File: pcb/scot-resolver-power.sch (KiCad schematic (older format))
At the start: 42 parts, among them IC4 TSR1, U1 MCP1703A-5002_SOT223, U2 LT1762, U3 MCP1703A-5002_SOT223, U4 MCP1703A-5002_SOT223, U5 MCP1703A-3302_SOT223

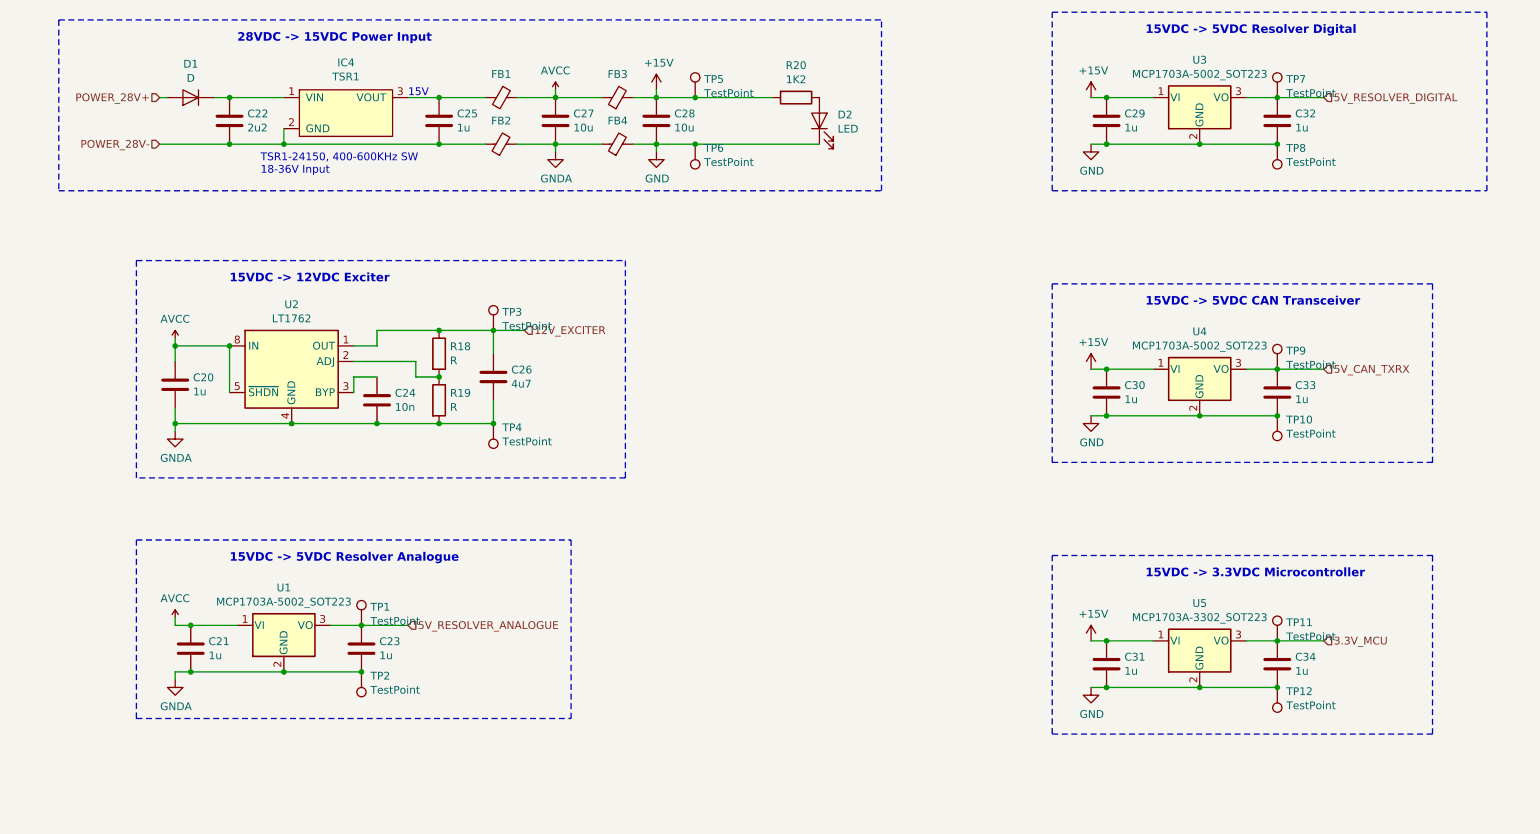
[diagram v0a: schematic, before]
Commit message: PCB Progress, laying tracks.
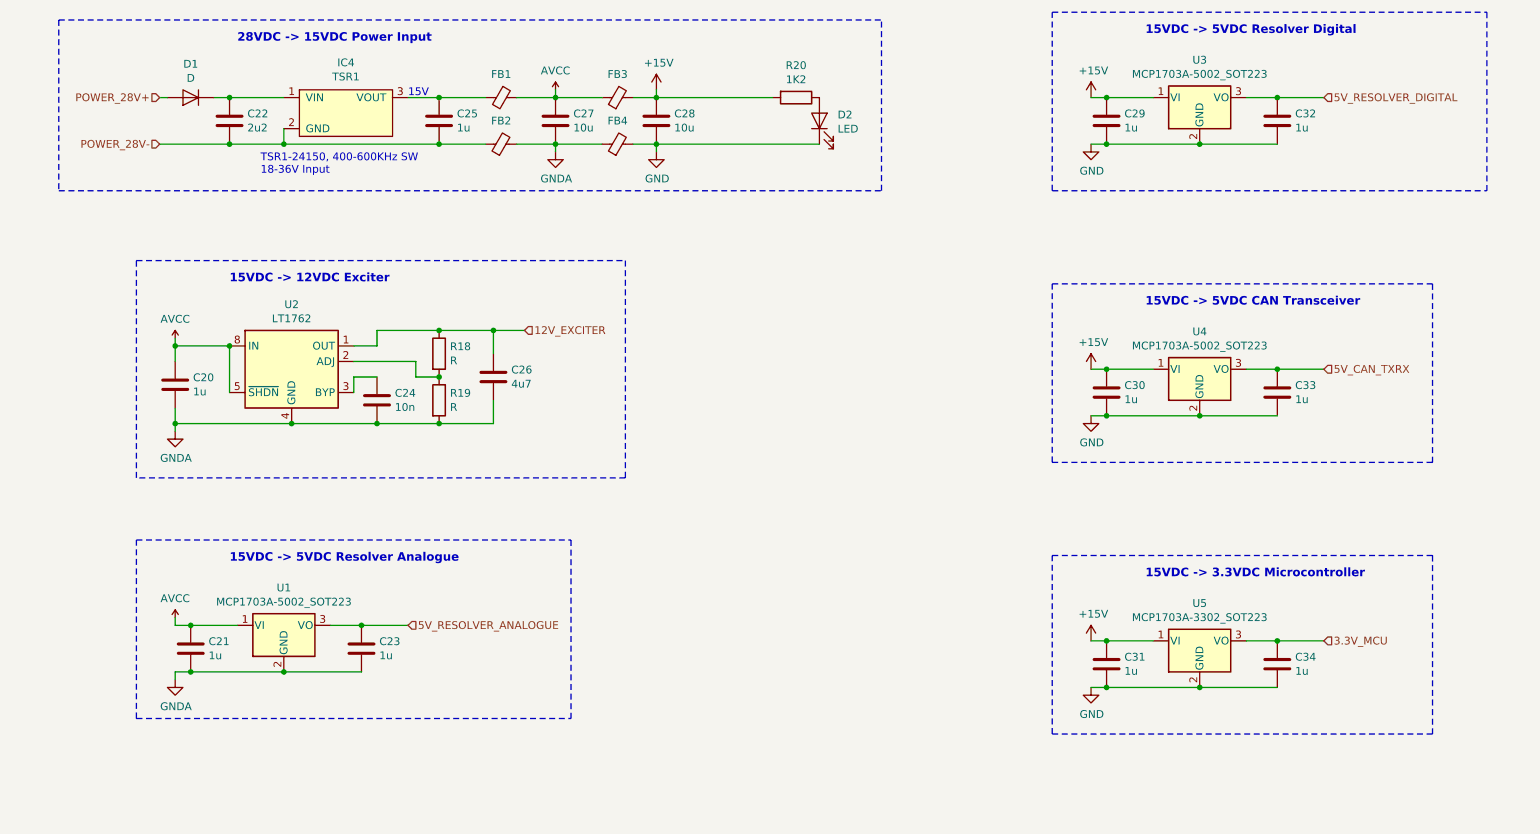
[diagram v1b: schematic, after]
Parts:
- removed TP1, TP10, TP11, TP12, TP2, TP3, TP4, TP5, TP6, TP7, TP8, TP9: TestPoint, TestPoint:TestPoint_Pad_D2.0mm, symbol Connector:TestPoint
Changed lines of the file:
@@
 Connection ~ 3250 3800
-Wire Wire Line
-	4000 3650 4000 3800
-Wire Wire Line
-	4000 3800 3650 3800
-Connection ~ 3650 3800
 Wire Wire Line
 	4000 3350 4000 3200
@@
 	1950 5100 1950 5050
 $Comp
-L Connector:TestPoint TP5
-U 1 1 5E584815
-P 5300 1700
-F 0 "TP5" H 5358 1818 50  0000 L CNN
-F 1 "TestPoint" H 5358 1727 50  0000 L CNN
-F 2 "TestPoint:TestPoint_Pad_D2.0mm" H 5500 1700 50  0001 C CNN
-F 3 "~" H 5500 1700 50  0001 C CNN
-	1    5300 1700
-	1    0    0    -1
-$EndComp
-$Comp
-L Connector:TestPoint TP6
-U 1 1 5E58568E
-P 5300 2000
-F 0 "TP6" H 5242 2026 50  0000 R CNN
-F 1 "TestPoint" H 5242 2117 50  0000 R CNN
-F 2 "TestPoint:TestPoint_Pad_D2.0mm" H 5500 2000 50  0001 C CNN
-F 3 "~" H 5500 2000 50  0001 C CNN
-	1    5300 2000
-	-1   0    0    1
-$EndComp
-Wire Wire Line
-	5050 2000 5300 2000
-Wire Wire Line
-	5050 1700 5300 1700
-$Comp
-L Connector:TestPoint TP3
-U 1 1 5E59AD0B
-P 4000 3200
-F 0 "TP3" H 4058 3318 50  0000 L CNN
-F 1 "TestPoint" H 4058 3227 50  0000 L CNN
-F 2 "TestPoint:TestPoint_Pad_D2.0mm" H 4200 3200 50  0001 C CNN
-F 3 "~" H 4200 3200 50  0001 C CNN
-	1    4000 3200
-	1    0    0    -1
-$EndComp
-$Comp
-L Connector:TestPoint TP4
-U 1 1 5E59B3ED
-P 4000 3800
-F 0 "TP4" H 3942 3826 50  0000 R CNN
-F 1 "TestPoint" H 3942 3917 50  0000 R CNN
-F 2 "TestPoint:TestPoint_Pad_D2.0mm" H 4200 3800 50  0001 C CNN
-F 3 "~" H 4200 3800 50  0001 C CNN
-	1    4000 3800
-	-1   0    0    1
-$EndComp
-Connection ~ 4000 3800
-$Comp
-L Connector:TestPoint TP1
-U 1 1 5E59C88E
-P 3150 5100
-F 0 "TP1" H 3208 5218 50  0000 L CNN
-F 1 "TestPoint" H 3208 5127 50  0000 L CNN
-F 2 "TestPoint:TestPoint_Pad_D2.0mm" H 3350 5100 50  0001 C CNN
-F 3 "~" H 3350 5100 50  0001 C CNN
-	1    3150 5100
-	1    0    0    -1
-$EndComp
-$Comp
-L Connector:TestPoint TP2
-U 1 1 5E59D052
-P 3150 5400
-F 0 "TP2" H 3092 5426 50  0000 R CNN
-F 1 "TestPoint" H 3092 5517 50  0000 R CNN
-F 2 "TestPoint:TestPoint_Pad_D2.0mm" H 3350 5400 50  0001 C CNN
-F 3 "~" H 3350 5400 50  0001 C CNN
-	1    3150 5400
-	-1   0    0    1
-$EndComp
-Connection ~ 3150 5400
-$Comp
-L Connector:TestPoint TP7
-U 1 1 5E59E980
-P 9050 1700
-F 0 "TP7" H 9108 1818 50  0000 L CNN
-F 1 "TestPoint" H 9108 1727 50  0000 L CNN
-F 2 "TestPoint:TestPoint_Pad_D2.0mm" H 9250 1700 50  0001 C CNN
-F 3 "~" H 9250 1700 50  0001 C CNN
-	1    9050 1700
-	1    0    0    -1
-$EndComp
-$Comp
-L Connector:TestPoint TP8
-U 1 1 5E5A080B
-P 9050 2000
-F 0 "TP8" H 8992 2026 50  0000 R CNN
-F 1 "TestPoint" H 8992 2117 50  0000 R CNN
-F 2 "TestPoint:TestPoint_Pad_D2.0mm" H 9250 2000 50  0001 C CNN
-F 3 "~" H 9250 2000 50  0001 C CNN
-	1    9050 2000
-	-1   0    0    1
-$EndComp
-Connection ~ 9050 2000
-$Comp
-L Connector:TestPoint TP10
-U 1 1 5E5A264B
-P 9050 3750
-F 0 "TP10" H 8992 3776 50  0000 R CNN
-F 1 "TestPoint" H 8992 3867 50  0000 R CNN
-F 2 "TestPoint:TestPoint_Pad_D2.0mm" H 9250 3750 50  0001 C CNN
-F 3 "~" H 9250 3750 50  0001 C CNN
-	1    9050 3750
-	-1   0    0    1
-$EndComp
-Connection ~ 9050 3750
-$Comp
-L Connector:TestPoint TP9
-U 1 1 5E5A2ECC
-P 9050 3450
-F 0 "TP9" H 9108 3568 50  0000 L CNN
-F 1 "TestPoint" H 9108 3477 50  0000 L CNN
-F 2 "TestPoint:TestPoint_Pad_D2.0mm" H 9250 3450 50  0001 C CNN
-F 3 "~" H 9250 3450 50  0001 C CNN
-	1    9050 3450
-	1    0    0    -1
-$EndComp
-$Comp
-L Connector:TestPoint TP12
-U 1 1 5E5A4134
-P 9050 5500
-F 0 "TP12" H 8992 5526 50  0000 R CNN
-F 1 "TestPoint" H 8992 5617 50  0000 R CNN
-F 2 "TestPoint:TestPoint_Pad_D2.0mm" H 9250 5500 50  0001 C CNN
-F 3 "~" H 9250 5500 50  0001 C CNN
-	1    9050 5500
-	-1   0    0    1
-$EndComp
-Connection ~ 9050 5500
-$Comp
-L Connector:TestPoint TP11
-U 1 1 5E5A4624
-P 9050 5200
-F 0 "TP11" H 9108 5318 50  0000 L CNN
-F 1 "TestPoint" H 9108 5227 50  0000 L CNN
-F 2 "TestPoint:TestPoint_Pad_D2.0mm" H 9250 5200 50  0001 C CNN
-F 3 "~" H 9250 5200 50  0001 C CNN
-	1    9050 5200
-	1    0    0    -1
-$EndComp
-$Comp
 L Device:LED D2
 U 1 1 5E5B0771
@@
 	0    1    1    0
 $EndComp
-Wire Wire Line
-	5800 1700 5300 1700
-Connection ~ 5300 1700
-Wire Wire Line
-	5300 2000 6100 2000
-Connection ~ 5300 2000
 Wire Notes Line
 	1200 2300 6500 2300
 Wire Notes Line
 	1200 1200 6500 1200
+Connection ~ 3650 3800
+Wire Wire Line
+	4000 3800 3650 3800
+Wire Wire Line
+	4000 3650 4000 3800
+Wire Wire Line
+	5050 1700 5800 1700
+Wire Wire Line
+	5050 2000 6100 2000
 $EndSCHEMATC

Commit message: Sent to fab (fab5)
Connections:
- net +15V: now also D2.2 (A); no longer R20.2
- net GND: now also R20.2; no longer D2.1 (K)
- net at R20.1: now also D2.1 (K); no longer D2.2 (A)
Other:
- moved on the sheet: D2, R20
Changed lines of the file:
@@
 L Device:LED D2
 U 1 1 5E5B0771
-P 6100 1850
-F 0 "D2" V 6139 1733 50  0000 R CNN
-F 1 "LED" V 6048 1733 50  0000 R CNN
-F 2 "Capacitor_SMD:C_1206_3216Metric_Pad1.42x1.75mm_HandSolder" H 6100 1850 50  0001 C CNN
-F 3 "~" H 6100 1850 50  0001 C CNN
-	1    6100 1850
+P 5900 1850
+F 0 "D2" V 5939 1733 50  0000 R CNN
+F 1 "LED" V 5848 1733 50  0000 R CNN
+F 2 "Capacitor_SMD:C_1206_3216Metric_Pad1.42x1.75mm_HandSolder" H 5900 1850 50  0001 C CNN
+F 3 "~" H 5900 1850 50  0001 C CNN
+	1    5900 1850
 	0    -1   -1   0
 $EndComp
@@
 L Device:R R20
 U 1 1 5E5B1516
-P 5950 1700
-F 0 "R20" V 5743 1700 50  0000 C CNN
-F 1 "1K2" V 5834 1700 50  0000 C CNN
-F 2 "Resistor_SMD:R_0805_2012Metric_Pad1.15x1.40mm_HandSolder" V 5880 1700 50  0001 C CNN
-F 3 "~" H 5950 1700 50  0001 C CNN
-	1    5950 1700
+P 5650 2000
+F 0 "R20" V 5443 2000 50  0000 C CNN
+F 1 "1K2" V 5534 2000 50  0000 C CNN
+F 2 "Resistor_SMD:R_0805_2012Metric_Pad1.15x1.40mm_HandSolder" V 5580 2000 50  0001 C CNN
+F 3 "~" H 5650 2000 50  0001 C CNN
+	1    5650 2000
 	0    1    1    0
 $EndComp
@@
 	4000 3650 4000 3800
 Wire Wire Line
-	5050 1700 5800 1700
+	5900 1700 5050 1700
 Wire Wire Line
-	5050 2000 6100 2000
+	5800 2000 5900 2000
+Wire Wire Line
+	5500 2000 5050 2000
 $EndSCHEMATC

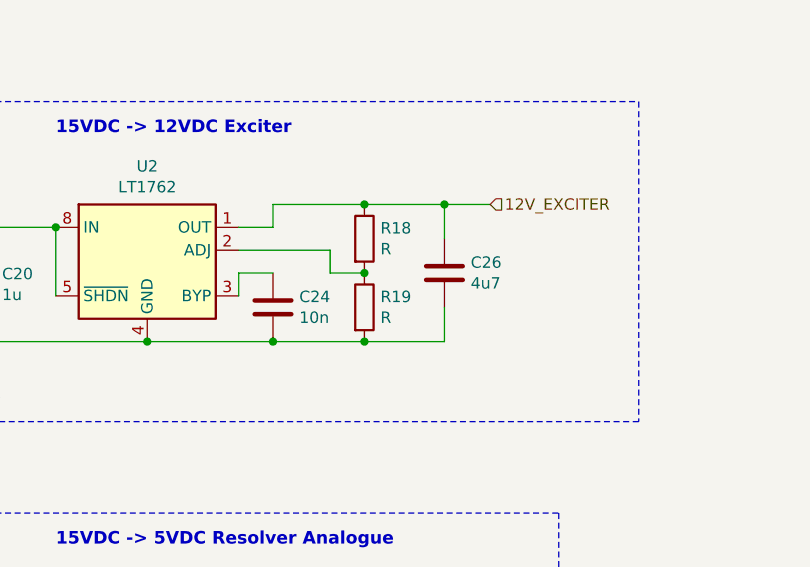
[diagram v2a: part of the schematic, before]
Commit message: pcb: Add labels and values to schematic.
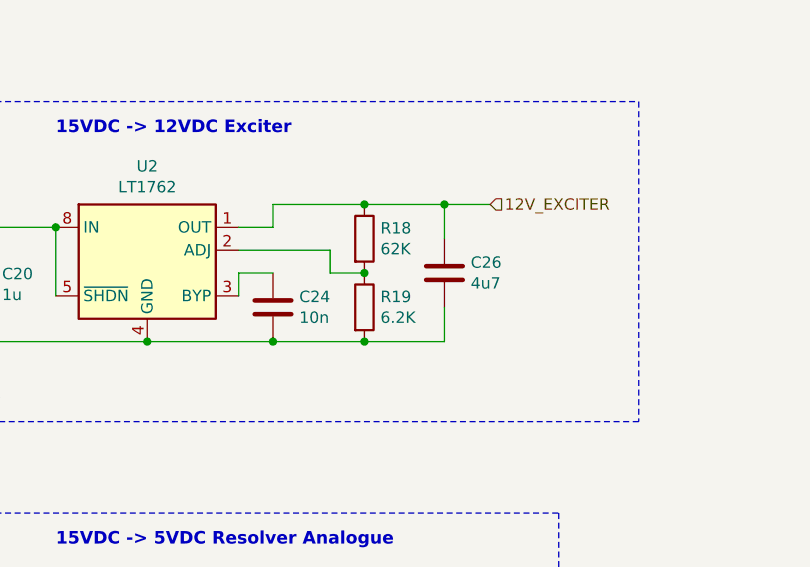
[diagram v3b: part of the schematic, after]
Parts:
- R18: value R -> 62K
- R19: value R -> 6.2K
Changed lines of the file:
@@
 AR Path="/5E2C28ED/5E2DB019" Ref="R19"  Part="1"
 F 0 "R19" H 3720 3696 50  0000 L CNN
-F 1 "R" H 3720 3605 50  0000 L CNN
+F 1 "6.2K" H 3720 3605 50  0000 L CNN
 F 2 "Resistor_SMD:R_0603_1608Metric_Pad1.05x0.95mm_HandSolder" V 3580 3650 50  0001 C CNN
 F 3 "~" H 3650 3650 50  0001 C CNN
@@
 AR Path="/5E2C28ED/5E2DB01F" Ref="R18"  Part="1"
 F 0 "R18" H 3720 3396 50  0000 L CNN
-F 1 "R" H 3720 3305 50  0000 L CNN
+F 1 "62K" H 3720 3305 50  0000 L CNN
 F 2 "Resistor_SMD:R_0603_1608Metric_Pad1.05x0.95mm_HandSolder" V 3580 3350 50  0001 C CNN
 F 3 "~" H 3650 3350 50  0001 C CNN

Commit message: WIP PCB v2.
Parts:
- removed D1: D, Diode_SMD:D_1206_3216Metric_Pad1.42x1.75mm_HandSolder, symbol Device:D
- added C?: 4u7/50V, Capacitor_SMD:C_1206_3216Metric_Pad1.42x1.75mm_HandSolder, symbol Device:C
- added C?: 4u7/50V, Capacitor_SMD:C_0603_1608Metric_Pad1.05x0.95mm_HandSolder, symbol Device:C
- added FB? (x2): 600R@100M/1A, Inductor_SMD:L_0805_2012Metric_Pad1.15x1.40mm_HandSolder, symbol Device:Ferrite_Bead_Small
- added R?: 240R/1%, Resistor_SMD:R_0805_2012Metric_Pad1.15x1.40mm_HandSolder, symbol Device:R
- added R?: 3K2/1%, Resistor_SMD:R_0805_2012Metric_Pad1.15x1.40mm_HandSolder, symbol Device:R
- added U?: LM317_3PinPackage, symbol Regulator_Linear:LM317_3PinPackage
- C21, C29, C30, C31: value 1u -> 1u/6.5V
- C22: value 2u2 -> 4u7/50V; footprint Capacitor_SMD:C_0603_1608Metric_Pad1.05x0.95mm_HandSolder -> Capacitor_SMD:C_1206_3216Metric_Pad1.42x1.75mm_HandSolder
- C23, C32, C33: value 1u -> 1u/5V
- C24: value 10n -> 10n/50V; footprint Capacitor_SMD:C_0402_1005Metric -> Capacitor_SMD:C_0603_1608Metric_Pad1.05x0.95mm_HandSolder
- C25: value 1u -> 4u7/6.5V
- C26: value 4u7 -> 4u7/50V
- C27, C28: value 10u -> 4u7/6.5V
- C34: value 1u -> 1u/3.3V
- FB1, FB2, FB3, FB4: value Ferrite_Bead_Small -> 600R@100M/1A
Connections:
- net POWER_28V+: now also C22.1, IC4.1 (VIN), C?.1, U?.3 (VI)
- net POWER_28V-: now also C?.2, C?.2, FB?.1, R?.2
- net +15V renamed DIGITAL_6.5V+
- net DIGITAL_6.5V+: now also C27.1, FB1.1, FB3.1; no longer C28.1, D2.2 (A), FB3.2
- net 12V_EXCITER renamed EXCITER_16V+
- removed net AVCC: C20.1, C21.1, C27.1, FB1.1, FB3.1, U1.1 (VI), U2.5 (~SHDN), U2.8 (IN)
- net GND renamed 0V_DIGITAL
- net 0V_DIGITAL: now also C27.2, FB2.2, FB4.1; no longer C28.2, FB4.2, R20.2
- removed net GNDA: C20.2, C21.2, C23.2, C24.2, C26.2, C27.2, FB2.2, FB4.1, R19.2, U1.2 (GND), U2.4 (GND)
- new net: C20.1, FB?.2, U2.5 (~SHDN), U2.8 (IN)
- new net: R?.1, R?.2, U?.1 (ADJ)
- new net: C?.1, FB?.1, R?.1, U?.2 (VO)
- new net 0V_ANALOG: C21.2, C23.2, C28.2, FB4.2, R20.2, U1.2 (GND)
- new net 0V_EXCITER: C20.2, C24.2, C26.2, FB?.2, R19.2, U2.4 (GND)
- new net ANALOG_6.5V+: C21.1, C28.1, D2.2 (A), FB3.2, U1.1 (VI)
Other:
- note added: "28VDC -> 16VDC Exciter"
- note added: "28VDC -> 6.5VDC Power Input"
- note added: "4V dropout for ideal RR"
- note added: "6.5VDC -> 3.3VDC Microcontroller"
- note added: "6.5VDC -> 5VDC CAN Transceiver"
- note added: "6.5VDC -> 5VDC Resolver Analog"
- note added: "6.5VDC -> 5VDC Resolver Digital"
- note added: "TSR1-2465, 400-600KHz SW\n9-32V Input"
- note added: "Vo = approx. 17.9V"
- note removed: "15VDC -> 12VDC Exciter"
- note removed: "15VDC -> 3.3VDC Microcontroller"
- note removed: "15VDC -> 5VDC CAN Transceiver"
- note removed: "15VDC -> 5VDC Resolver Analogue"
- note removed: "15VDC -> 5VDC Resolver Digital"
- note removed: "28VDC -> 15VDC Power Input"
- note removed: "TSR1-24150, 400-600KHz SW\n18-36V Input"
- moved on the sheet: C20, C21, C22, C23, C24, C25, C26, C28, C29, C30, C31, C32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
